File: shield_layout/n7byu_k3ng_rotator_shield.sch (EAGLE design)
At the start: 26 parts, among them J1 ARDUINO_R3_SHIELD

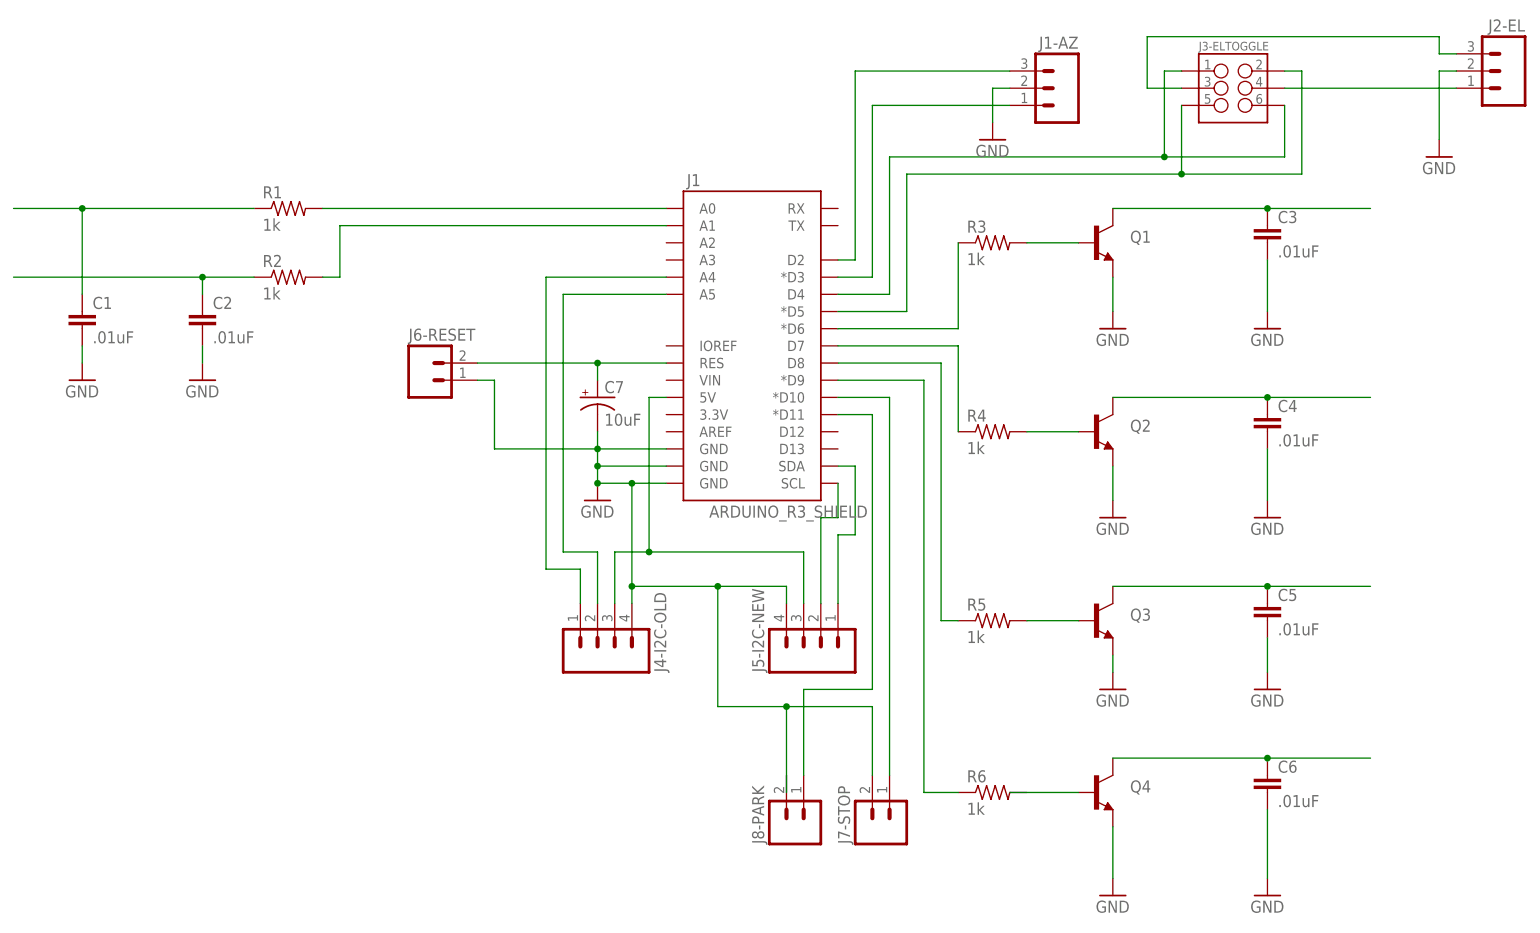
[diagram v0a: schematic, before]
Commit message: attempt to clear pins D10-D11, to make it compatible with a standard Ethernet shield Still needs testing
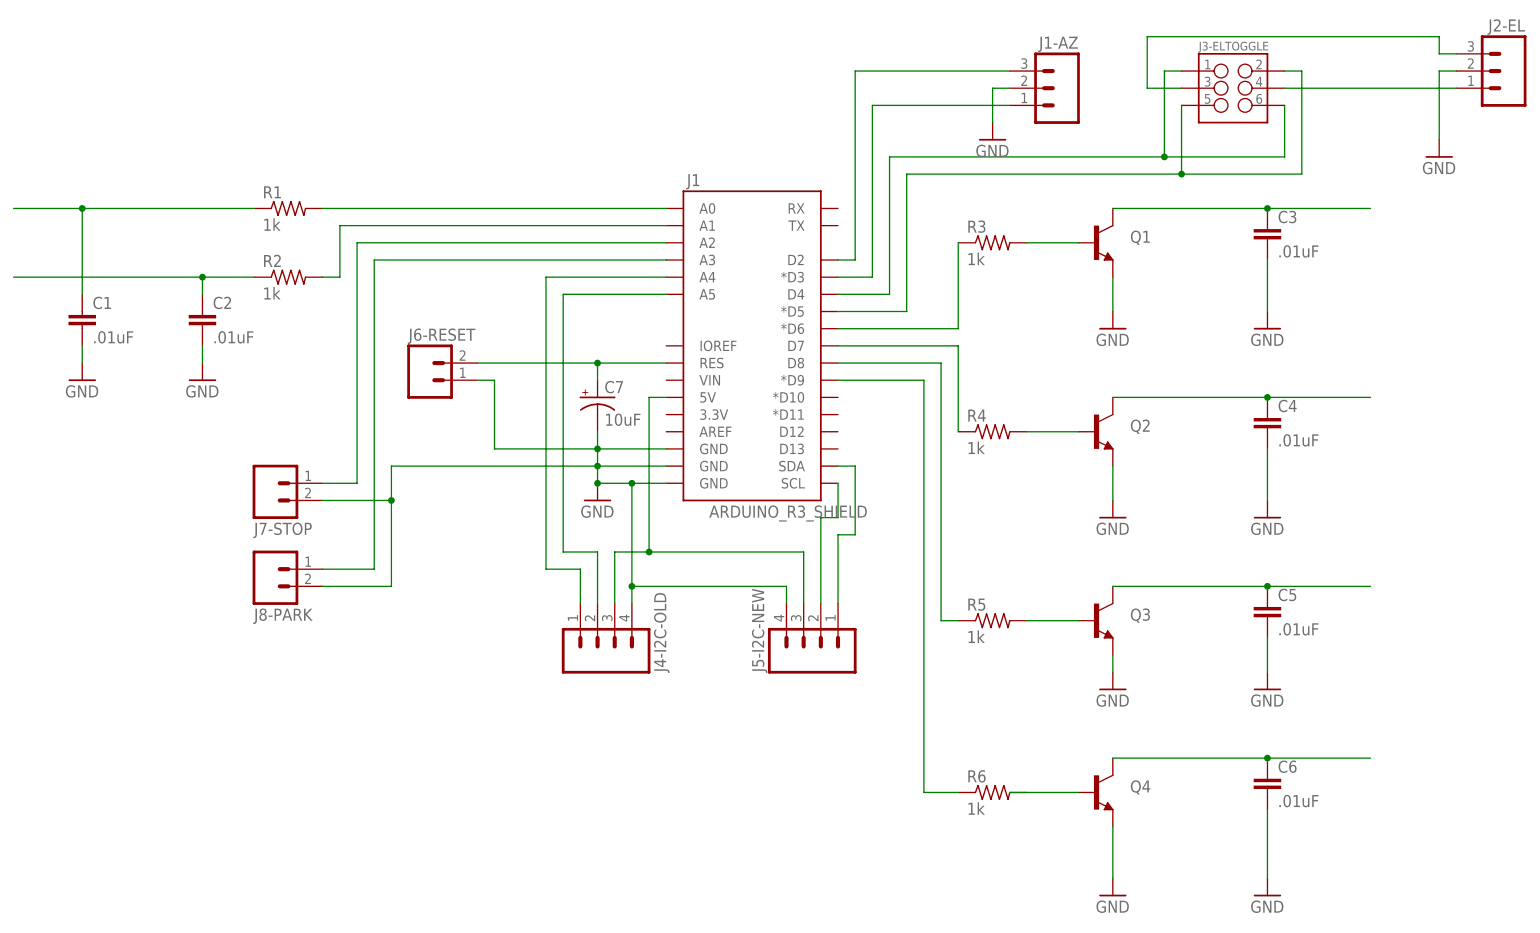
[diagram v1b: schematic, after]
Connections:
- removed net N$29: J1.*D11, J8-PARK.1
- new net N$31: J1.A3, J8-PARK.1
- net GND: now also J8-PARK.2
- net N$28: now also J1.A2; no longer J1.*D10
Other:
- moved on the sheet: J7-STOP, J8-PARK
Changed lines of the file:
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@@
 <instance part="J5-I2C-NEW" gate="G$1" x="119.38" y="7.62" rot="R90"/>
 <instance part="J6-RESET" gate="G$1" x="60.96" y="45.72"/>
-<instance part="J7-STOP" gate="G$1" x="129.54" y="-20.32" rot="R90"/>
-<instance part="J8-PARK" gate="G$1" x="116.84" y="-20.32" rot="R90"/>
+<instance part="J7-STOP" gate="G$1" x="38.1" y="30.48" rot="MR180"/>
+<instance part="J8-PARK" gate="G$1" x="38.1" y="17.78" rot="MR180"/>
 </instances>
 <busses>
@@
 <junction x="86.36" y="30.48"/>
 <pinref part="J4-I2C-OLD" gate="G$1" pin="4"/>
-<wire x1="114.3" y1="15.24" x2="104.14" y2="15.24" width="0.1524" layer="91"/>
-<wire x1="104.14" y1="15.24" x2="91.44" y2="15.24" width="0.1524" layer="91"/>
+<wire x1="114.3" y1="15.24" x2="91.44" y2="15.24" width="0.1524" layer="91"/>
 <wire x1="91.44" y1="15.24" x2="91.44" y2="12.7" width="0.1524" layer="91"/>
 <wire x1="91.44" y1="15.24" x2="91.44" y2="30.48" width="0.1524" layer="91"/>
@@
 <pinref part="J5-I2C-NEW" gate="G$1" pin="4"/>
 <wire x1="114.3" y1="15.24" x2="114.3" y2="12.7" width="0.1524" layer="91"/>
-<pinref part="J7-STOP" gate="G$1" pin="2"/>
-<wire x1="127" y1="-12.7" x2="127" y2="-2.54" width="0.1524" layer="91"/>
-<wire x1="127" y1="-2.54" x2="114.3" y2="-2.54" width="0.1524" layer="91"/>
-<wire x1="114.3" y1="-15.24" x2="114.3" y2="-2.54" width="0.1524" layer="91"/>
-<wire x1="114.3" y1="-2.54" x2="104.14" y2="-2.54" width="0.1524" layer="91"/>
-<junction x="114.3" y="-2.54"/>
-<wire x1="104.14" y1="-2.54" x2="104.14" y2="15.24" width="0.1524" layer="91"/>
-<junction x="104.14" y="15.24"/>
 <pinref part="J6-RESET" gate="G$1" pin="1"/>
 <wire x1="68.58" y1="45.72" x2="71.12" y2="45.72" width="0.1524" layer="91"/>
 <wire x1="71.12" y1="45.72" x2="71.12" y2="35.56" width="0.1524" layer="91"/>
 <wire x1="71.12" y1="35.56" x2="86.36" y2="35.56" width="0.1524" layer="91"/>
+<pinref part="J7-STOP" gate="G$1" pin="2"/>
+<wire x1="45.72" y1="27.94" x2="55.88" y2="27.94" width="0.1524" layer="91"/>
+<wire x1="55.88" y1="27.94" x2="55.88" y2="33.02" width="0.1524" layer="91"/>
+<wire x1="55.88" y1="33.02" x2="86.36" y2="33.02" width="0.1524" layer="91"/>
+<pinref part="J8-PARK" gate="G$1" pin="2"/>
+<wire x1="45.72" y1="15.24" x2="55.88" y2="15.24" width="0.1524" layer="91"/>
+<wire x1="55.88" y1="15.24" x2="55.88" y2="27.94" width="0.1524" layer="91"/>
+<junction x="55.88" y="27.94"/>
 </segment>
 <segment>
@@
 <net name="N$28" class="0">
 <segment>
-<pinref part="J1" gate="G$1" pin="*D10"/>
-<wire x1="121.92" y1="43.18" x2="129.54" y2="43.18" width="0.1524" layer="91"/>
 <pinref part="J7-STOP" gate="G$1" pin="1"/>
-<wire x1="129.54" y1="43.18" x2="129.54" y2="-12.7" width="0.1524" layer="91"/>
-</segment>
-</net>
-<net name="N$29" class="0">
-<segment>
-<pinref part="J1" gate="G$1" pin="*D11"/>
-<wire x1="121.92" y1="40.64" x2="127" y2="40.64" width="0.1524" layer="91"/>
-<wire x1="127" y1="40.64" x2="127" y2="0" width="0.1524" layer="91"/>
-<wire x1="127" y1="0" x2="116.84" y2="0" width="0.1524" layer="91"/>
+<wire x1="45.72" y1="30.48" x2="50.8" y2="30.48" width="0.1524" layer="91"/>
+<wire x1="50.8" y1="30.48" x2="50.8" y2="66.04" width="0.1524" layer="91"/>
+<pinref part="J1" gate="G$1" pin="A2"/>
+<wire x1="50.8" y1="66.04" x2="96.52" y2="66.04" width="0.1524" layer="91"/>
+</segment>
+</net>
+<net name="N$31" class="0">
+<segment>
 <pinref part="J8-PARK" gate="G$1" pin="1"/>
-<wire x1="116.84" y1="0" x2="116.84" y2="-12.7" width="0.1524" layer="91"/>
-</segment>
-</net>
+<wire x1="45.72" y1="17.78" x2="53.34" y2="17.78" width="0.1524" layer="91"/>
+<wire x1="53.34" y1="17.78" x2="53.34" y2="63.5" width="0.1524" layer="91"/>
+<pinref part="J1" gate="G$1" pin="A3"/>
+<wire x1="53.34" y1="63.5" x2="96.52" y2="63.5" width="0.1524" layer="91"/>
+</segment>
+</net>
